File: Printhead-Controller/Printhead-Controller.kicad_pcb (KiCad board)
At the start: 2 copper layers, 93.7 x 73 mm, 61 parts, among them J1 Serial Prog, J2 OLED Screen, J3 2 x 10 Pinheader, J4 USB_B_Micro, Q1 AO3400A, SW1 Rotary_Encoder, SW2 USER1, SW3 BOOT, SW4 RESET, U1 ESP32-WROOM-32D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

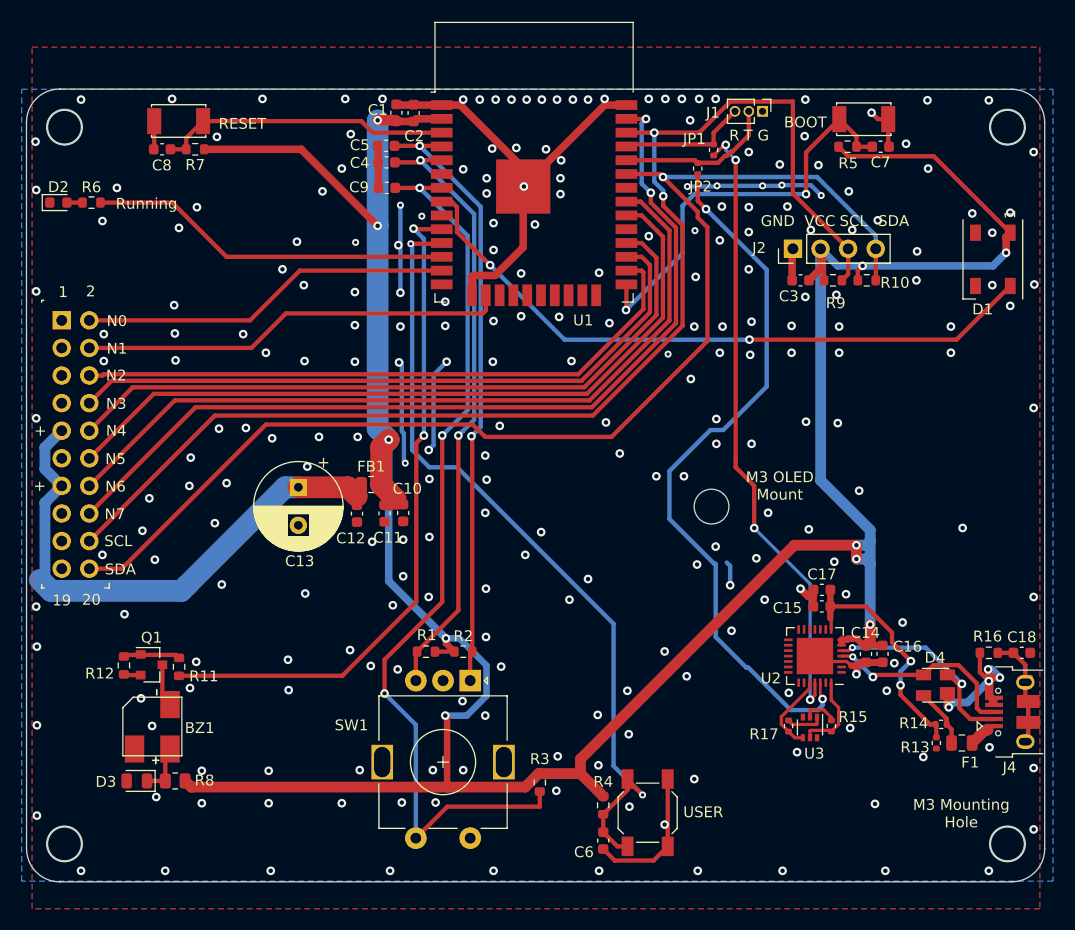
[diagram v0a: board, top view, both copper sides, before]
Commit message: final PCB KiCAD design files for V0.5 as sent off for manufacture at JLCPCB 2022-03-22
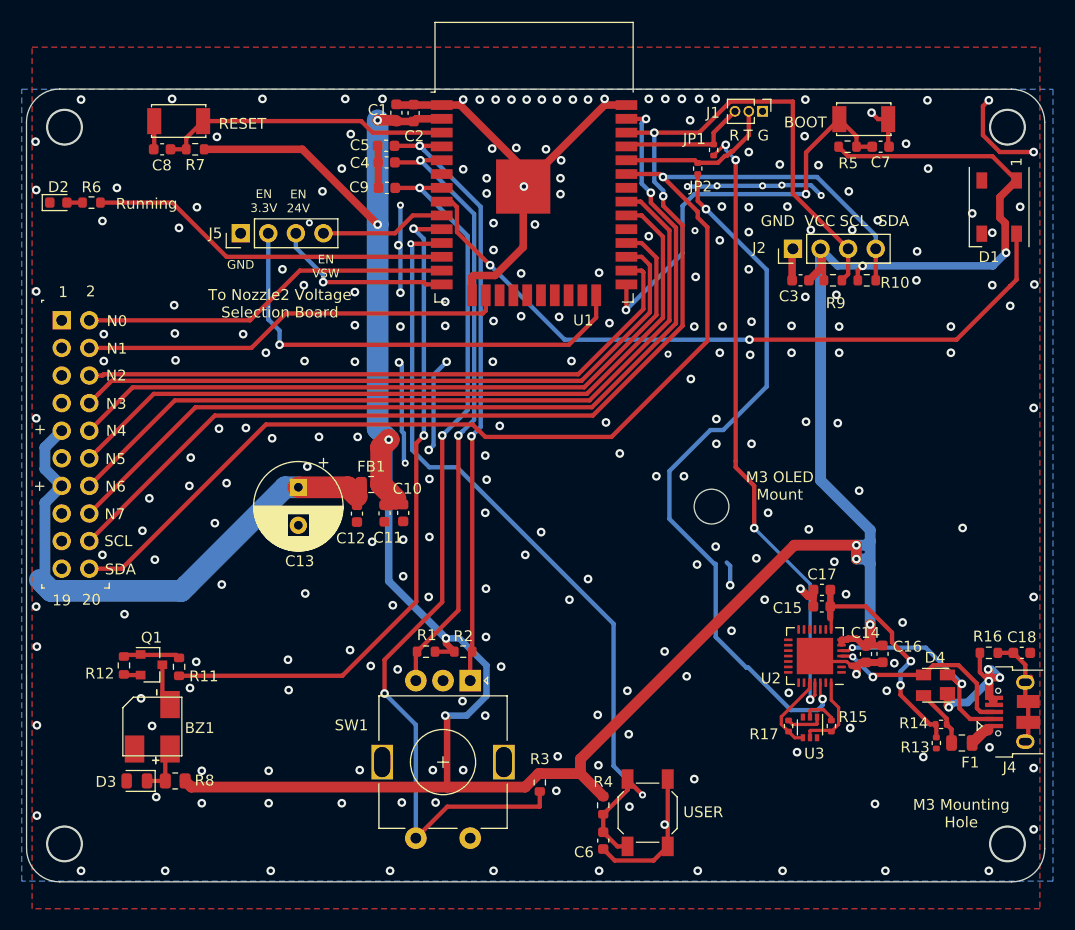
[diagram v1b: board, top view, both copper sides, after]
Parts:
- added J5: Nozzle2 Board (Future), Connector_PinHeader_2.54mm:PinHeader_1x04_P2.54mm_Vertical, F.Cu at (122.2, 67.5)
- moved D1 4.85 mm to (192.0, 65.1)
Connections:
- U1 pad 14: (no net) -> EN_24V
- U1 pad 24: (no net) -> EN_3.3V
- U1 pad 9: (no net) -> EN_VSW
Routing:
- net EN_3.3V: track 0.00 -> 42.9 mm, vias 0 -> 1
- net EN_24V: track 0.00 -> 16.5 mm, vias 0 -> 1
- net EN_VSW: track 0.00 -> 11.6 mm
- net GND: track 142.4 -> 151.1 mm, vias 254 -> 252
- net RGB: track 61.0 -> 66.0 mm
- net +3V3: track 274.2 -> 278.3 mm
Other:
- board text added: "EN 24V"
- board text added: "EN 3.3V"
- board text added: "EN VSW"
- board text added: "To Nozzle2 Volatge Selection Board"
- board text added: "To Nozzle2 Voltage Selection Board"

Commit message: Updating Controller and Driver boards to version 0.6
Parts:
- removed JP1, JP2: Jumper_NC_Small, Resistor_SMD:R_0402_1005Metric
- added J2: Plug, Connector_Hirose:Hirose_DF13C_CL535-0403-5-51_1x03-1MP_P1.25mm_Vertical, F.Cu at (126.3, 57.2)
- added TP1: TestPoint, TestPoint:TestPoint_THTPad_1.5x1.5mm_Drill0.7mm, F.Cu at (132.1, 61.5)
- J3: value 2 x 10 Pinheader -> Header; footprint Connector_PinSocket_2.54mm:PinSocket_2x10_P2.54mm_Vertical -> Connector_PinHeader_2.54mm:PinHeader_1x03_P2.54mm_Vertical; moved to F.Cu
- J5: value Nozzle2 Board (Future) -> Conn_02x12_Odd_Even; footprint Connector_PinHeader_2.54mm:PinHeader_1x04_P2.54mm_Vertical -> Connector_PinHeader_2.54mm:PinHeader_2x12_P2.54mm_Vertical
- R13, R14, R15, R17: footprint Resistor_SMD:R_0402_1005Metric -> Resistor_SMD:R_0603_1608Metric
- moved D1 84.8 mm to (107.4, 69.0), turned to 0 degrees
- moved J3 26.9 mm to (128.9, 61.9), turned to 270 degrees
- moved J5 18.3 mm to (105.7, 75.5), turned to 0 degrees
- moved R8 7.00 mm to (118.5, 111.3), turned to 90 degrees
- moved D3 6.71 mm to (118.5, 114.7), turned to 270 degrees
- moved R13 0.51 mm to (186.1, 114.9)
- moved R15 0.27 mm to (176.8, 113.0)
- moved H5 0.27 mm to (165.5, 92.9)
- moved R17 0.25 mm to (172.4, 112.9)
- moved R14 0.10 mm to (186.7, 112.6)
- renumbered J2 to J4, J4 to J6
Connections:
- J3 pad 2: PH0 -> DAC2
- J3 pad 3: GND -> +3V3
- J5 pad 2: EN_3.3V -> PH0
- J5 pad 3: EN_24V -> GND
- J5 pad 4: EN_VSW -> PH1
- U1 pad 11: USER1 -> DAC2
- U1 pad 14: EN_24V -> SCLK
- U1 pad 23: (no net) -> MOSI
- U1 pad 24: EN_3.3V -> MISO
- U1 pad 29: (no net) -> CS
- U1 pad 6: (no net) -> Net-(TP1-Pad1)
- U1 pad 9: EN_VSW -> USER1
- U2 pad 25: Net-(JP1-Pad1) -> Rx
- U2 pad 26: Net-(JP2-Pad1) -> Tx
- U3 pad 3: (no net) -> RESET
- U3 pad 6: (no net) -> BOOT
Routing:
- net SDA: track 112.7 -> 29.4 mm
- net SCL: track 117.0 -> 35.3 mm, vias 2 -> 0
- net CS: track 0.00 -> 75.9 mm, vias 0 -> 1
- net RESET: track 27.1 -> 97.3 mm, vias 0 -> 2
- net Net-(JP2-Pad1): track 66.5 -> 0.00 mm, vias 2 -> 0
- net Tx: track 14.6 -> 80.0 mm, vias 0 -> 2
- net MISO: track 0.00 -> 61.1 mm, vias 0 -> 1
- net GND: track 151.1 -> 211.7 mm, vias 252 -> 265
- net Rx: track 12.0 -> 70.5 mm, vias 0 -> 3
- net MOSI: track 0.00 -> 58.1 mm, vias 0 -> 1
- net Net-(JP1-Pad1): track 57.6 -> 0.00 mm, vias 4 -> 0
- net BOOT: track 38.7 -> 95.9 mm, vias 2 -> 4
- net EN_3.3V: track 42.9 -> 0.00 mm, vias 1 -> 0
- net SCLK: track 0.00 -> 42.6 mm, vias 0 -> 1
- net RGB: track 66.0 -> 32.5 mm
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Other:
- board text added: "23"
- board text added: "24"
- board text added: "CS"
- board text added: "GPIO26"
- board text added: "GPIO27: LED"
- board text added: "GPIO33: User SW"
- board text added: "IO12: SCLK"
- board text added: "IO15: MOSI"
- board text added: "IO26"
- board text added: "IO2: MISO"
- board text added: "IO34: TP1"
- board text added: "IO5: CS"
- board text added: "MISO"
- board text added: "MOSI"
- board text added: "PRL V0.6"
- board text added: "S/N:"
- board text added: "SCLK"
- board text added: "Serial Port"
- board text removed: "19"
- board text removed: "20"
- board text removed: "EN 24V"
- board text removed: "EN 3.3V"
- board text removed: "EN VSW"
- board text removed: "GPIO27L LED"
- board text removed: "IO21: SDA"
- board text removed: "IO22: SCL"
- board text removed: "PRL V0.5"
- board text removed: "To Nozzle2 Volatge Selection Board"
- board text removed: "To Nozzle2 Voltage Selection Board"

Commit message: Adding in version 0.7 KiACD design files
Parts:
- added H6: MH-M2, MountingHole:MountingHole_2.2mm_M2, F.Cu at (162.0, 110.2)
- R15, R17: value 12K -> 10K
- moved J4 0.06 mm to (173.0, 68.9)
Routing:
- net +3V3: track 288.9 -> 290.0 mm
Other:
- board text added: "M2 Mounting Hole"
- board text added: "PRL V0.7"
- board text removed: "PRL V0.6"
